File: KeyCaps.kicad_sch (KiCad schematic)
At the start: 48 parts

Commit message: Major changes
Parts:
- renumbered C3 to C301, C3 to C302, C3 to C303, C3 to C304, C3 to C305, C3 to C306, C3 to C307, C3 to C308, C3 to C309, C3 to C310, C3 to C311, C3 to C312, C3 to C313, C3 to C314, C3 to C315, C3 to C316, R2 to R301, R2 to R302, R2 to R303, R2 to R304, R2 to R305, R2 to R306, R2 to R307, R2 to R308, R2 to R309, R2 to R310, R2 to R311, R2 to R312, R2 to R313, R2 to R314, R2 to R315, R2 to R316
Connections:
- no-connect marks 0 -> 1
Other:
- moved on the sheet: C302, C303

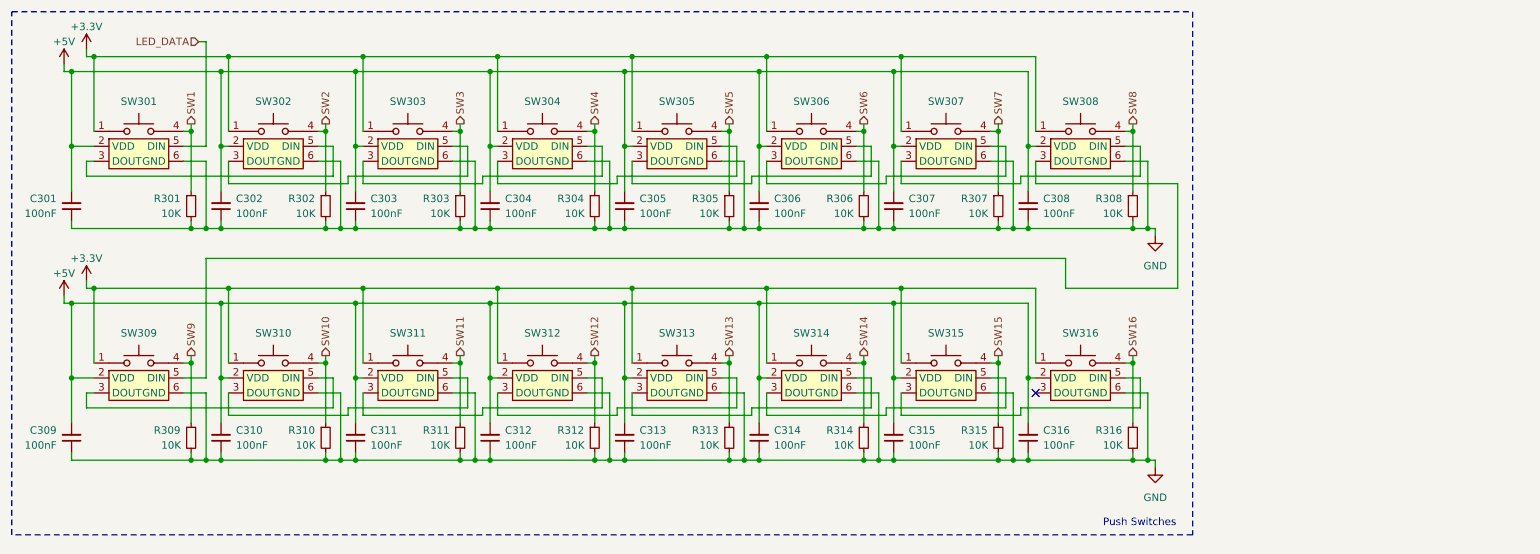
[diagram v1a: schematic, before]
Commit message: Fixed wiring for buttons
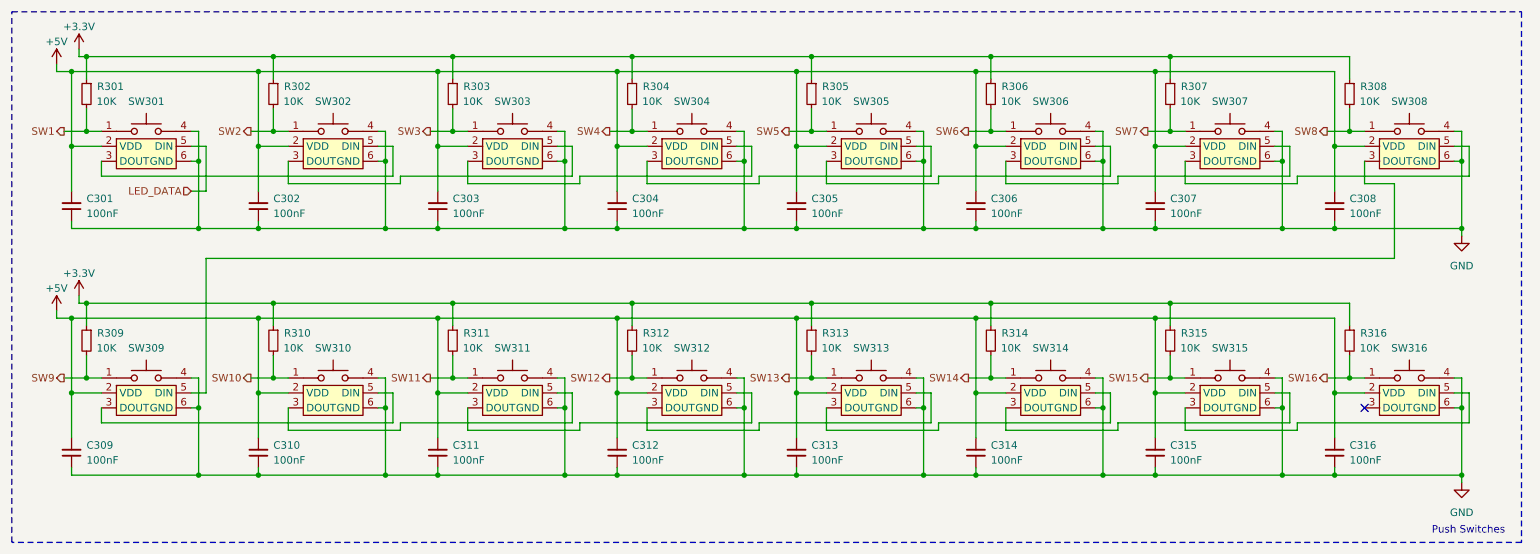
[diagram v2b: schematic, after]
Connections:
- net +3.3V: now also R301.1, R302.1, R303.1, R304.1, R305.1, R306.1, R307.1, R308.1, R309.1, R310.1, R311.1, R312.1, R313.1, R314.1, R315.1, R316.1; no longer SW301.1, SW302.1, SW303.1, SW304.1, SW305.1, SW306.1, SW307.1, SW308.1, SW309.1, SW310.1, SW311.1, SW312.1, SW313.1, SW314.1, SW315.1, SW316.1
- net GND: now also SW301.4, SW302.4, SW303.4, SW304.4, SW305.4, SW306.4, SW307.4, SW308.4, SW309.4, SW310.4, SW311.4, SW312.4, SW313.4, SW314.4, SW315.4, SW316.4; no longer R301.2, R302.2, R303.2, R304.2, R305.2, R306.2, R307.2, R308.2, R309.2, R310.2, R311.2, R312.2, R313.2, R314.2, R315.2, R316.2
- net SW1: now also R301.2, SW301.1; no longer R301.1, SW301.4
- net SW10: now also R310.2, SW310.1; no longer R310.1, SW310.4
- net SW11: now also R311.2, SW311.1; no longer R311.1, SW311.4
- net SW12: now also R312.2, SW312.1; no longer R312.1, SW312.4
- net SW13: now also R313.2, SW313.1; no longer R313.1, SW313.4
- net SW14: now also R314.2, SW314.1; no longer R314.1, SW314.4
- net SW15: now also R315.2, SW315.1; no longer R315.1, SW315.4
- net SW16: now also R316.2, SW316.1; no longer R316.1, SW316.4
- net SW2: now also R302.2, SW302.1; no longer R302.1, SW302.4
- net SW3: now also R303.2, SW303.1; no longer R303.1, SW303.4
- net SW4: now also R304.2, SW304.1; no longer R304.1, SW304.4
- net SW5: now also R305.2, SW305.1; no longer R305.1, SW305.4
- net SW6: now also R306.2, SW306.1; no longer R306.1, SW306.4
- net SW7: now also R307.2, SW307.1; no longer R307.1, SW307.4
- net SW8: now also R308.2, SW308.1; no longer R308.1, SW308.4
- net SW9: now also R309.2, SW309.1; no longer R309.1, SW309.4
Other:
- moved on the sheet: C301, C302, C303, C304, C305, C306, C307, C308, R301, R302, R303, R304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
